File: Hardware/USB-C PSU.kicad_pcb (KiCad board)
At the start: 8 copper layers, 50 x 50 mm, 158 parts, among them J1 USB_C_Receptacle_USB2.0_16P, J101 USB_C_Receptacle_USB2.0_16P, J102 ST7789 LCD, J103 TC2030, J104 Expansion, J2 VOUT, J3 TC2030, J4 VIN, Q1 100V 50A, Q101 AO3400A, Q2 100V 50A, Q3 100V 50A, Q4 100V 50A, SW1 SW_Reverse, SW101 SIQ-02FVS3, SW102 SW_Back, SW103 Reset, SW104 Boot, SW2 Boot, SW3 Reset, U1 CH32X035G8U6, U101 CH32X035G8U6, U102 AP2112K-3.3, U103 TPS22915CYFPR, U104 SIT3088ETK, U105 LIS3DH, U2 BQ25758A, U4 LMR51610XDBVR, U5 TPD4S480RUKR, U6 TPS22915CYFPR, U7 TPS22915CYFPR

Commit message: final tweaks before routing traces
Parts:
- added TP21: TestPoint, TestPoint:TestPoint_Pad_D1.0mm, F.Cu at (101.7, 78.5)
- C14: value 1u 25V -> 4u7u 25V
- moved C110 21.1 mm to (116.2, 110.0)
- moved C107 0.95 mm to (127.8, 114.4)
- moved R111 0.95 mm to (126.8, 114.4)
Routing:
- net /C_D-: track 2.86 -> 0.00 mm
- net /C_D+: track 2.83 -> 0.00 mm
- net Net-(U5-RPD_G1): track 2.24 -> 0.00 mm
- net Net-(U5-RPD_G2): track 1.22 -> 0.00 mm

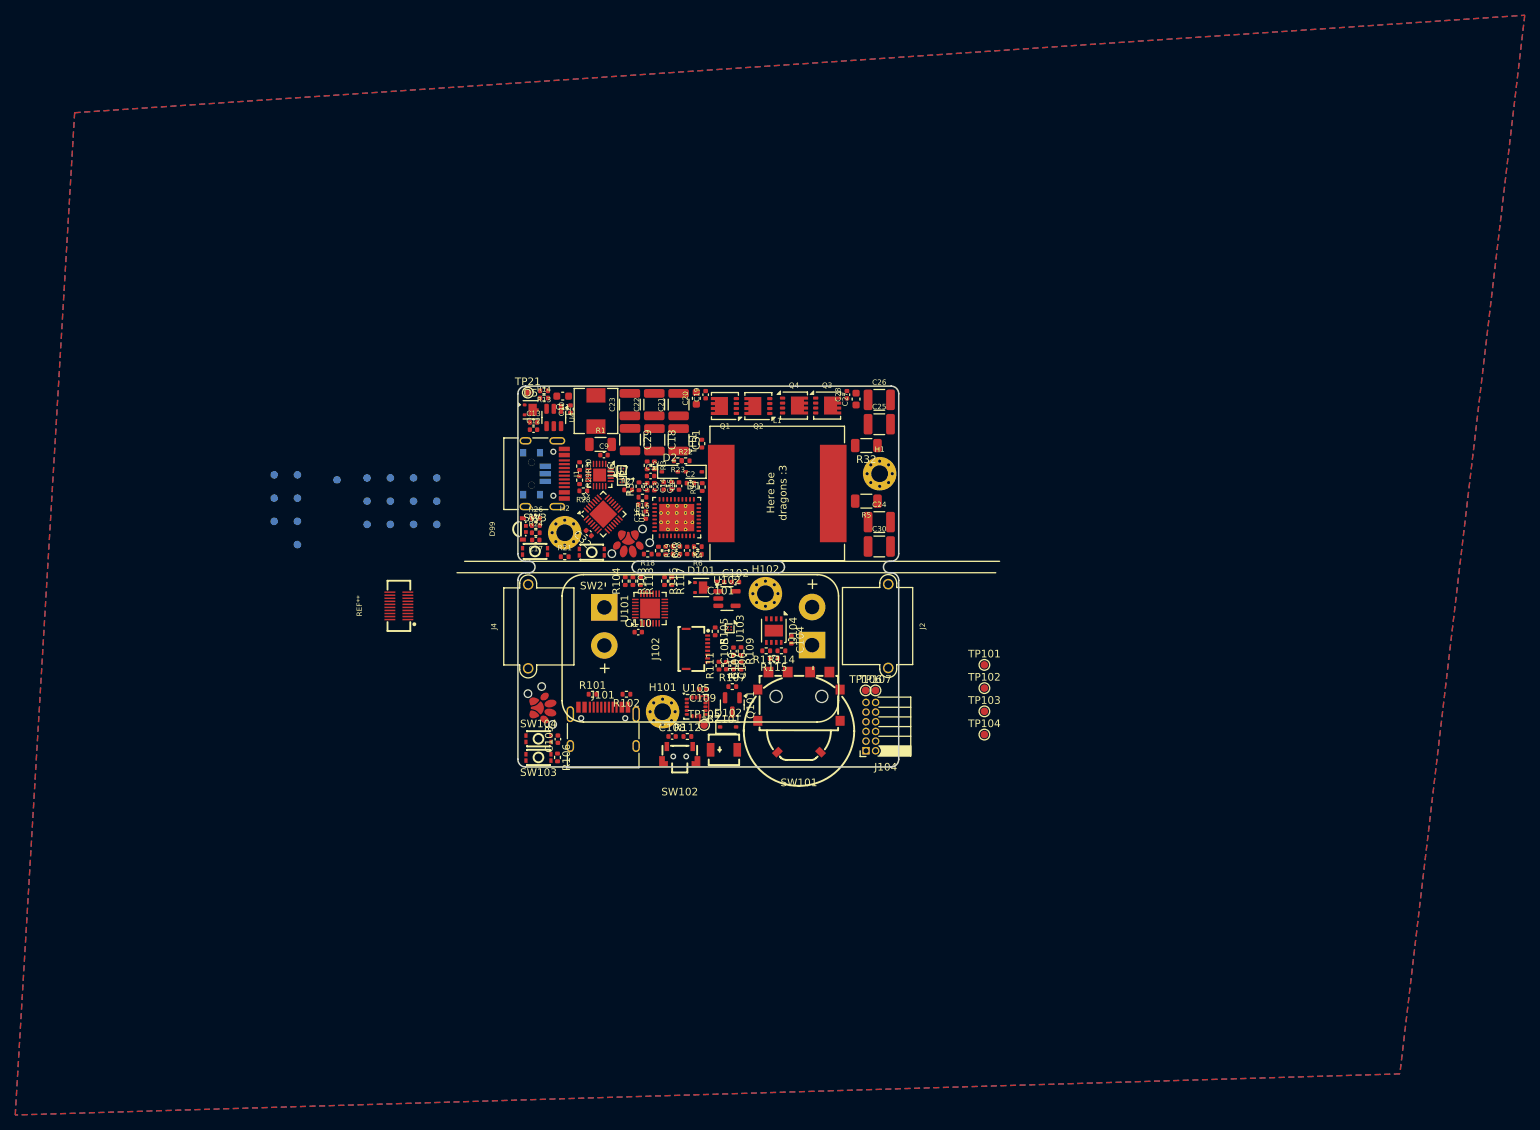
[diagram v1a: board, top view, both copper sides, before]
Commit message: main power layout almost done
UI board and details still left to do
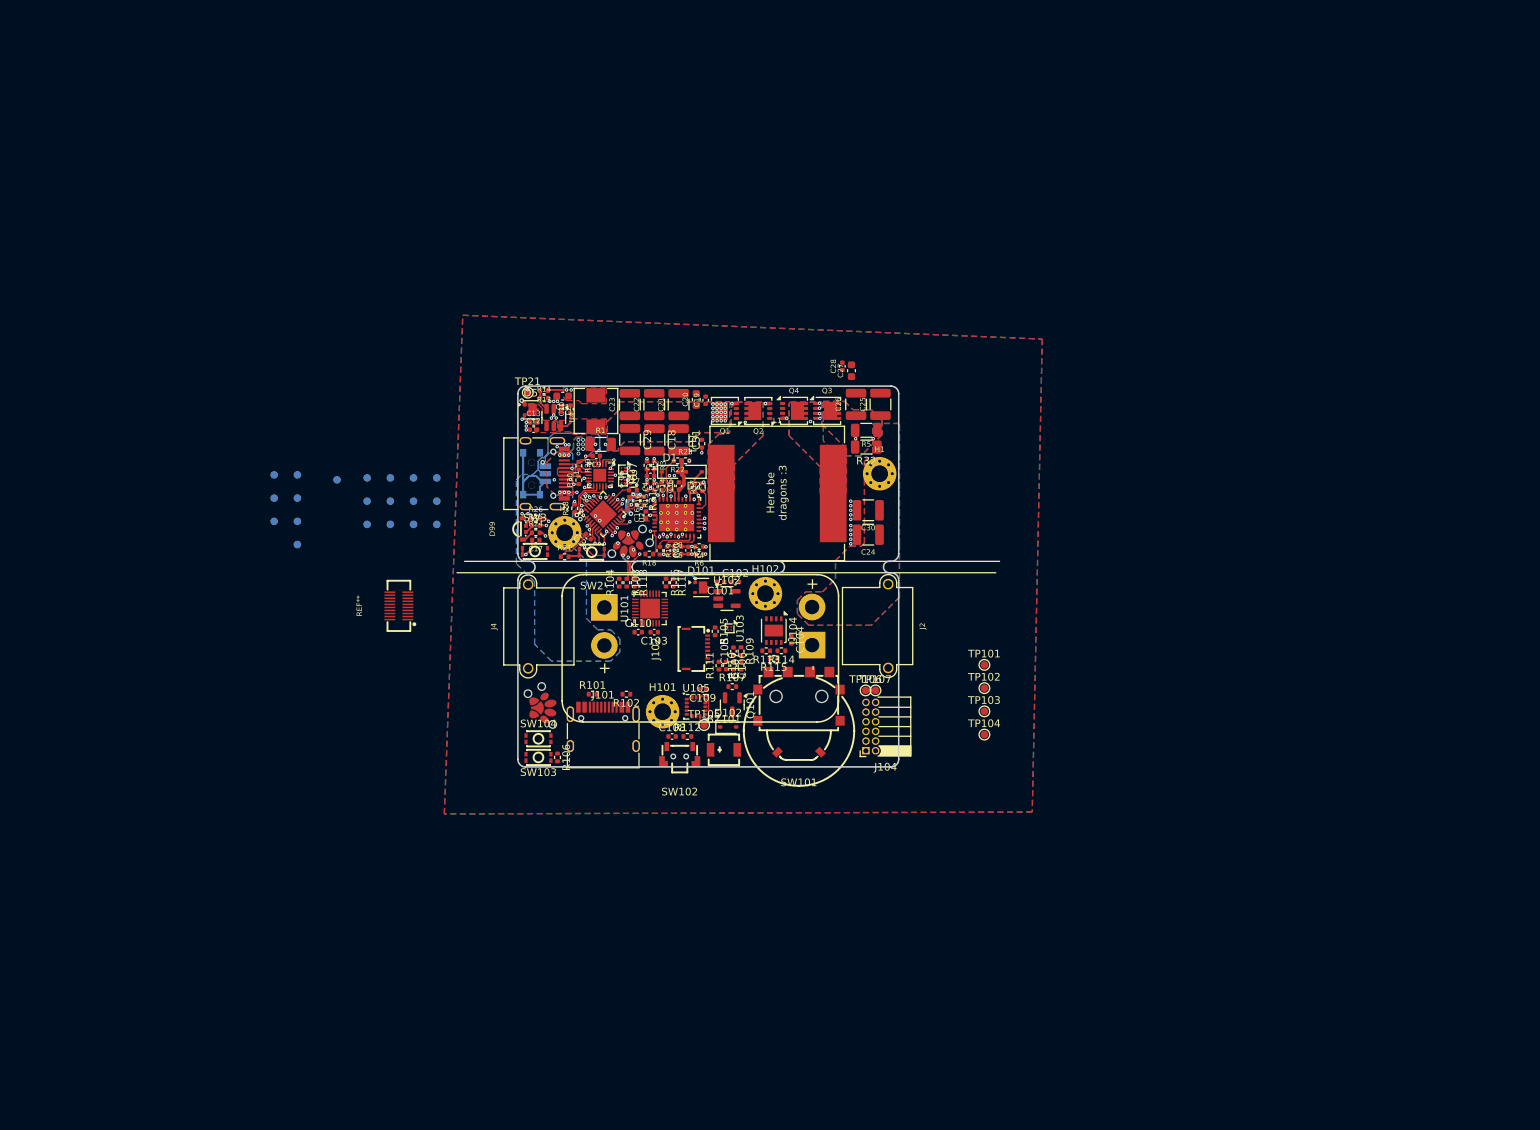
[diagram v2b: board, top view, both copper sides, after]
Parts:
- moved C103 18.9 mm to (118.3, 110.0), turned to 180 degrees
- moved R5 9.30 mm to (146.2, 83.5)
- moved C30 4.97 mm to (146.4, 94.0), turned to 180 degrees
- moved C27 3.77 mm to (144.2, 75.7)
- moved C28 3.77 mm to (143.0, 75.1)
- moved D1 3.15 mm to (120.3, 89.0), turned to 0 degrees
- moved D2 3.15 mm to (123.5, 89.0), turned to 180 degrees
- moved C26 3.11 mm to (144.8, 80.1), turned to 90 degrees
- moved C25 2.60 mm to (148.0, 80.1), turned to 90 degrees
- moved R28 2.57 mm to (107.8, 93.8), turned to 90 degrees
- moved C24 2.20 mm to (146.4, 97.2), turned to 180 degrees
- moved R31 2.01 mm to (117.0, 92.8), turned to -90 degrees
- moved R29 1.90 mm to (108.4, 88.2)
- moved R30 1.85 mm to (108.4, 90.0), turned to 90 degrees
- moved R16 1.76 mm to (115.0, 92.8), turned to -90 degrees
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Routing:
- net VOUT: track 0.00 -> 110.9 mm, vias 0 -> 4
- net +5V: track 0.00 -> 103.2 mm, vias 0 -> 15
- net VBUS: track 0.00 -> 40.5 mm, vias 0 -> 21
- net CAP_VOUT: track 0.00 -> 29.2 mm, vias 0 -> 2
- net Net-(R27-Pad2): track 0.00 -> 24.0 mm, vias 0 -> 2
- net NTC: track 0.00 -> 23.9 mm, vias 0 -> 3
- net RESET: track 0.00 -> 23.7 mm, vias 0 -> 3
- net /DCDC Converter/HIDRV2: track 0.00 -> 22.0 mm, vias 0 -> 2
- net /DCDC Converter/SW2: track 0.00 -> 20.9 mm, vias 0 -> 5
- net /DCDC Converter/LODRV1: track 0.00 -> 19.2 mm, vias 0 -> 2
- net /DCDC Converter/LODRV2: track 0.00 -> 18.5 mm, vias 0 -> 2
- net /DCDC Converter/HIDRV1: track 0.00 -> 18.3 mm, vias 0 -> 2
- net /DCDC Converter/SW1: track 0.00 -> 17.7 mm, vias 0 -> 2
- net LED_B: track 0.00 -> 16.8 mm, vias 0 -> 2
- net D+: track 0.00 -> 16.0 mm, vias 0 -> 2
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- added copper zone on F.Cu, net +5V
- added copper zone on F.Cu, net /BUCK_VIN
- added copper zone on B.Cu, net /DCDC Converter/SW1
- added copper zone on F.Cu, net /DCDC Converter/SW1
- added copper zone on In2.Cu, net /DCDC Converter/SW1
- added copper zone on In3.Cu, net /DCDC Converter/SW1
- added copper zone on In4.Cu, net /DCDC Converter/SW1
- added copper zone on In5.Cu, net /DCDC Converter/SW1
- added copper zone on B.Cu, net /DCDC Converter/SW2
- added copper zone on F.Cu, net /DCDC Converter/SW2
- added copper zone on In3.Cu, net /DCDC Converter/SW2
- added copper zone on In4.Cu, net /DCDC Converter/SW2
- added copper zone on In5.Cu, net /DCDC Converter/SW2
- added copper zone on B.Cu, net CAP_VIN
- added copper zone on F.Cu, net CAP_VIN
- added copper zone on In3.Cu, net CAP_VIN
- added copper zone on In4.Cu, net CAP_VIN
- added copper zone on In5.Cu, net CAP_VIN
- added copper zone on B.Cu, net CAP_VOUT
- added copper zone on F.Cu, net CAP_VOUT
- added copper zone on In3.Cu, net CAP_VOUT
- added copper zone on In4.Cu, net CAP_VOUT
- added copper zone on In5.Cu, net CAP_VOUT
- added copper zone on In2.Cu, net GND
- added copper zone on In5.Cu, net GND
- added copper zone on F.Cu, net Net-(U4-SW)
- added copper zone on B.Cu, net VBUS
- added copper zone on F.Cu, net VBUS
- added copper zone on In2.Cu, net VBUS
- added copper zone on In3.Cu, net VBUS
- added copper zone on In4.Cu, net VBUS
- added copper zone on In5.Cu, net VBUS
- added copper zone on In6.Cu, net VBUS
- added copper zone on B.Cu, net VOUT
- added copper zone on F.Cu, net VOUT
- added copper zone on In1.Cu, net VOUT
- added copper zone on In2.Cu, net VOUT
- added copper zone on In3.Cu, net VOUT
- added copper zone on In4.Cu, net VOUT
- added copper zone on In5.Cu, net VOUT
- added copper zone on In6.Cu, net VOUT

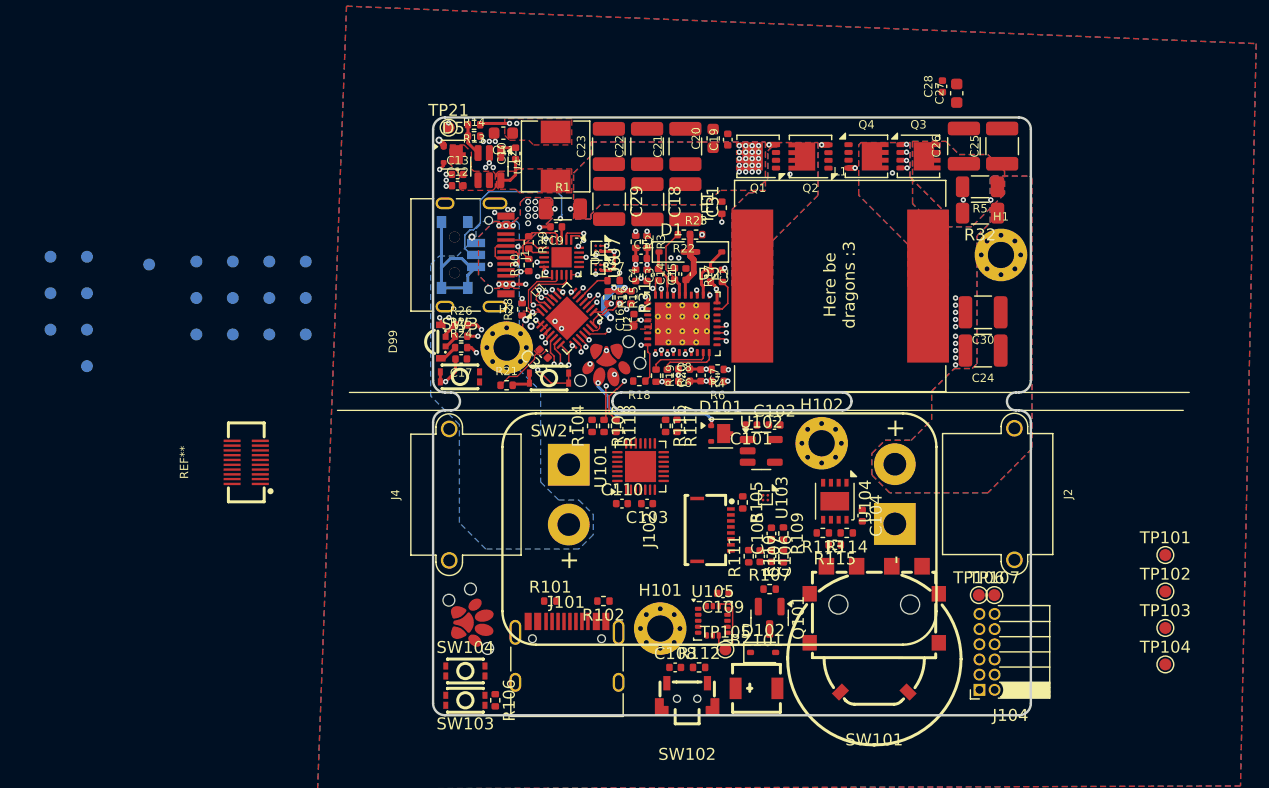
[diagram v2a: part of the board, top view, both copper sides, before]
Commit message: UI layout done
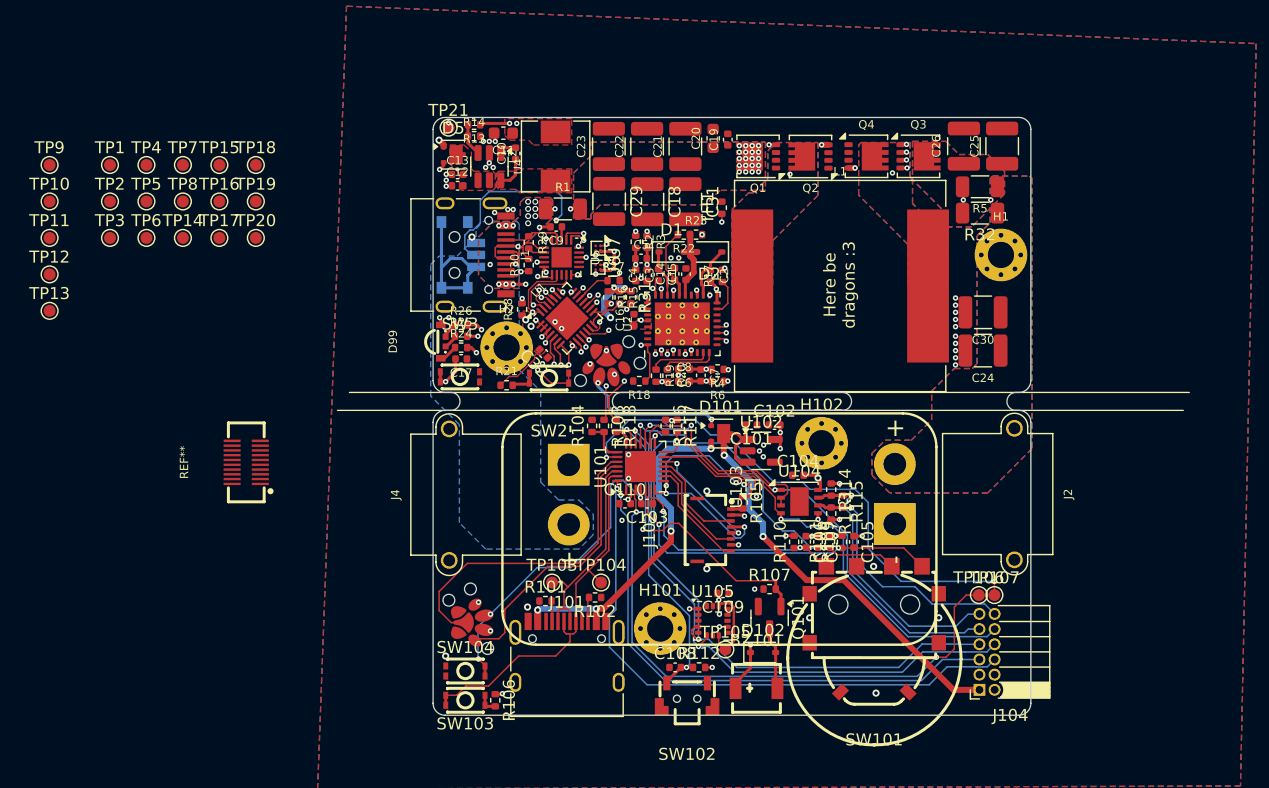
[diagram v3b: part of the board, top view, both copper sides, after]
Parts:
- removed C27: 1u 100V, Capacitor_SMD:C_0603_1608Metric
- removed C28: 100n 100V, Capacitor_SMD:C_0402_1005Metric
- removed TP101, TP102: TestPoint, TestPoint:TestPoint_Pad_D1.0mm
- TP1, TP10, TP11, TP12, TP13, TP14, TP15, TP16, TP17, TP18, TP19, TP2, TP20, TP3, TP4, TP5, TP6, TP7, TP8, TP9: moved to F.Cu
- moved TP103 51.4 mm to (110.3, 116.6)
- moved TP104 47.7 mm to (114.5, 116.6)
- moved TP9 20.9 mm to (68.3, 81.7), turned to 0 degrees
- moved TP19 18.8 mm to (85.6, 84.7), turned to 0 degrees
- moved TP18 18.8 mm to (85.6, 81.7), turned to 0 degrees
- moved TP20 18.8 mm to (85.6, 87.8), turned to 0 degrees
- moved TP1 18.3 mm to (73.4, 81.7), turned to 0 degrees
- moved TP2 18.3 mm to (73.4, 84.7), turned to 0 degrees
- moved TP3 18.3 mm to (73.4, 87.8), turned to 0 degrees
- moved TP15 15.4 mm to (82.5, 81.7), turned to 0 degrees
- moved TP16 15.4 mm to (82.5, 84.7), turned to 0 degrees
- moved TP17 15.4 mm to (82.5, 87.8), turned to 0 degrees
- moved TP10 13.3 mm to (68.3, 84.7), turned to 0 degrees
- moved TP11 13.3 mm to (68.3, 87.8), turned to 0 degrees
- moved TP12 13.3 mm to (68.3, 90.8), turned to 0 degrees
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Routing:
- net UI_SCL: track 0.00 -> 49.2 mm, vias 0 -> 2
- net UI_SDA: track 0.00 -> 49.0 mm, vias 0 -> 2
- net UI_PC14: track 0.00 -> 48.6 mm, vias 0 -> 1
- net UI_PC0: track 0.00 -> 48.1 mm, vias 0 -> 2
- net UI_PC15: track 0.00 -> 44.9 mm, vias 0 -> 1
- net UI_PB12: track 0.00 -> 44.9 mm, vias 0 -> 2
- net UI_VIN: track 0.00 -> 39.8 mm, vias 0 -> 2
- net RS485_RO: track 0.00 -> 38.8 mm, vias 0 -> 1
- net RS485_DI: track 0.00 -> 36.8 mm, vias 0 -> 1
- net UI_D+: track 0.00 -> 31.9 mm
- net ENC_BTN: track 0.00 -> 29.4 mm, vias 0 -> 2
- net ENC_A: track 0.00 -> 28.5 mm, vias 0 -> 2
- net UI_VBUS: track 0.00 -> 28.2 mm, vias 0 -> 4
- net UI_RESET: track 0.00 -> 26.9 mm, vias 0 -> 3
- net BUZZER: track 0.00 -> 26.2 mm, vias 0 -> 2
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- added copper zone on In5.Cu, net +3V3
- added copper zone on In5.Cu, net +5V

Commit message: oops, all vias
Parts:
- removed C12: 100n 100V, Capacitor_SMD:C_0402_1005Metric
- removed TP10: ACOV, TestPoint:TestPoint_Pad_D1.0mm
- removed TP13: FSW_SYNC, TestPoint:TestPoint_Pad_D1.0mm
- removed TP14, TP15, TP3, TP4: TestPoint, TestPoint:TestPoint_Pad_D1.0mm
- removed TP9: ACUV, TestPoint:TestPoint_Pad_D1.0mm
- C11: value 22u -> 22u 10V
- C13: value 4u7 100V -> 1u 100V; footprint Capacitor_SMD:C_0402_1005Metric -> Capacitor_SMD:C_0603_1608Metric
- TP1, TP11, TP12, TP16, TP17, TP18, TP19, TP2, TP20, TP5, TP6, TP7, TP8: moved to B.Cu
- moved TP11 45.4 mm to (113.2, 94.5), turned to 180 degrees
- moved TP12 43.5 mm to (111.8, 91.5), turned to 180 degrees
- moved TP5 36.6 mm to (111.9, 93.8), turned to 180 degrees
- moved TP1 36.4 mm to (107.7, 93.8), turned to 180 degrees
- moved TP2 35.2 mm to (108.2, 89.6), turned to 180 degrees
- moved TP6 34.4 mm to (110.3, 93.8), turned to 180 degrees
- moved TP7 32.6 mm to (111.1, 89.7), turned to 180 degrees
- moved TP16 32.0 mm to (111.9, 97.3), turned to 180 degrees
- moved TP8 31.8 mm to (111.1, 88.0), turned to 180 degrees
- moved TP18 29.8 mm to (111.9, 95.7), turned to 180 degrees
- moved TP17 29.4 mm to (110.3, 97.3), turned to 180 degrees
- moved TP20 27.3 mm to (110.3, 99.3), turned to 180 degrees
- moved TP19 27.1 mm to (110.3, 95.7), turned to 180 degrees
- moved C13 0.57 mm to (102.2, 83.0)
- moved R21 0.20 mm to (106.5, 99.9)
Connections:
- J3 pad 6: unconnected-(J3-SWO-Pad6) -> TX
- J3 pad 7: (no net) -> RX
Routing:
- net Net-(U2-STAT): track 0.21 -> 13.5 mm
- net Net-(U2-~{PG}/STAT3): track 0.14 -> 10.8 mm
- net PA7: track 2.06 -> 8.60 mm
- net DCDC_EN: track 11.6 -> 16.4 mm
- net PA6: track 0.66 -> 4.67 mm
- net VCONN2_EN: track 7.27 -> 10.6 mm
- net VCONN1_EN: track 3.51 -> 6.87 mm
- net RX: track 14.0 -> 17.2 mm, vias 2 -> 3
- net PA4: track 1.04 -> 4.05 mm
- net GND: track 19.2 -> 22.2 mm, vias 57 -> 191
- net DCDC_INT: track 9.57 -> 12.0 mm
- net CC2: track 14.1 -> 15.9 mm
- net PA5: track 0.95 -> 2.73 mm
- net /DCDC Converter/LODRV1: track 19.2 -> 20.5 mm
- net CC1: track 15.4 -> 16.5 mm
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- added copper zone on In2.Cu, net CAP_VIN
- added copper zone on In1.Cu, net VBUS
